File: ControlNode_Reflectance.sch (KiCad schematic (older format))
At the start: 0 parts

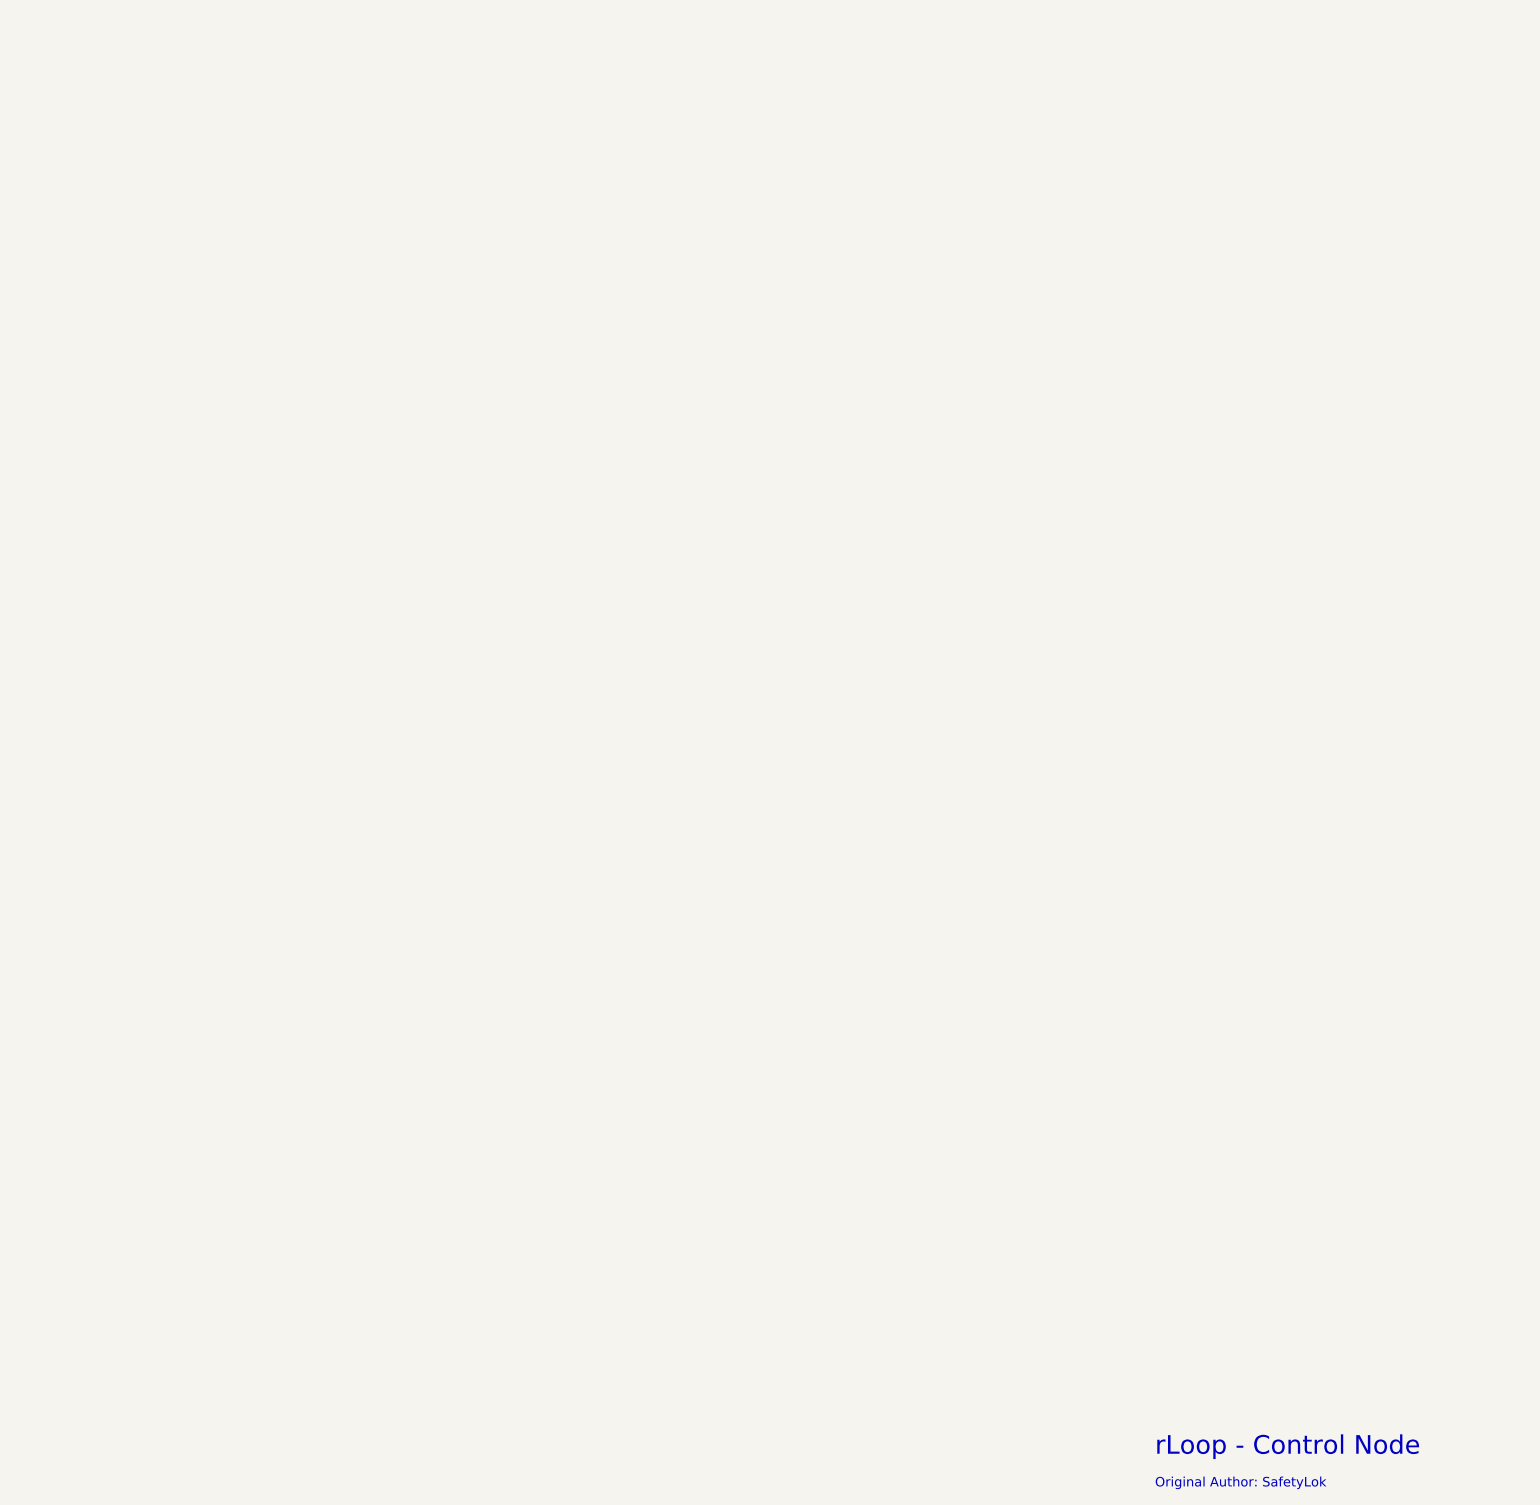
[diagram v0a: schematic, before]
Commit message: Update height sensors.
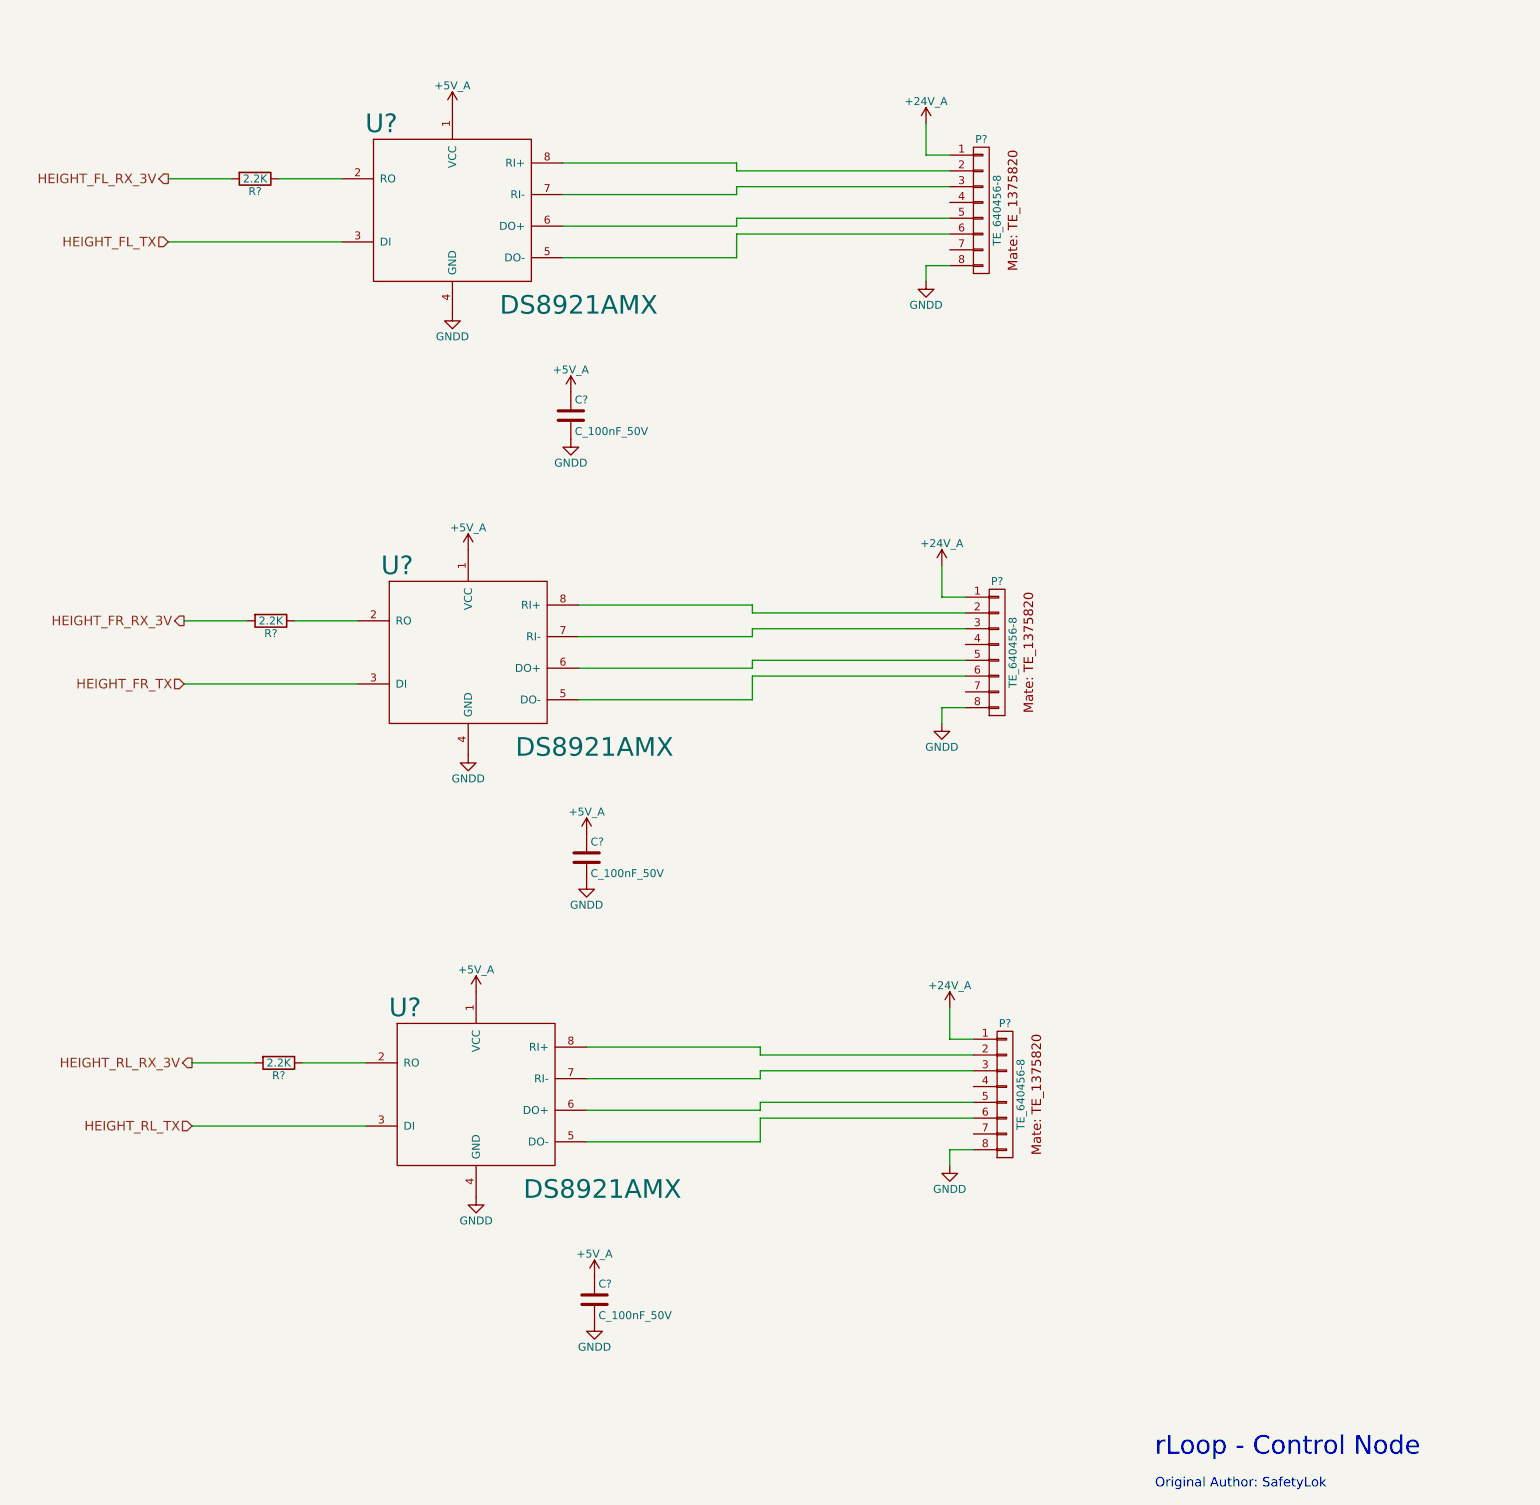
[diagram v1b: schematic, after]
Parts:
- added C? (x3): C_100nF_50V, RLOOP_FOOTPRINTS:rLoop_C_0603, symbol C_100nF_50V
- added P? (x3): TE_640456-8, RLOOP_FOOTPRINTS:rLoop_TE640456-8, symbol TE_640456-8
- added R? (x3): 2.2K, RLOOP_FOOTPRINTS:rLoop_R_0603, symbol 2.2K
- added U? (x3): DS8921AMX, RLOOP_FOOTPRINTS:rLoop_SOIC8, symbol DS8921AMX
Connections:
- new net: P?.2 (P2), U?.8 (RI+) (x3)
- new net: P?.3 (P3), U?.7 (RI-) (x3)
- new net: P?.5 (P5), U?.6 (DO+) (x3)
- new net: P?.6 (P6), U?.5 (DO-) (x3)
- new net: R?.1, U?.2 (RO) (x3)
- new net +5V: C?.1, C?.1, C?.1, P?.1 (P1), P?.1 (P1), P?.1 (P1), U?.1 (VCC), U?.1 (VCC), U?.1 (VCC)
- new net GNDD: C?.2, C?.2, C?.2, P?.8 (P8), P?.8 (P8), P?.8 (P8), U?.4 (GND), U?.4 (GND), U?.4 (GND)
- new net HEIGHT_FL_RX_3V: R?.2
- new net HEIGHT_FL_TX: U?.3 (DI)
- new net HEIGHT_FR_RX_3V: R?.2
- new net HEIGHT_FR_TX: U?.3 (DI)
- new net HEIGHT_RL_RX_3V: R?.2
- new net HEIGHT_RL_TX: U?.3 (DI)

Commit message: Release 1
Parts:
- removed C? (x3): C_100nF_50V, RLOOP_FOOTPRINTS:rLoop_C_0603, symbol C_100nF_50V
- removed P? (x3): TE_640456-8, RLOOP_FOOTPRINTS:rLoop_TE640456-8, symbol TE_640456-8
- removed R? (x3): 2.2K, RLOOP_FOOTPRINTS:rLoop_R_0603, symbol 2.2K
- removed U? (x3): DS8921AMX, RLOOP_FOOTPRINTS:rLoop_SOIC8, symbol DS8921AMX
- added C?: C_100nF_50V, RLOOP_FOOTPRINTS:rLoop_C_0603, symbol C_100nF_50V
- added P? (x3): TE_640456-8, RLOOP_FOOTPRINTS:rLoop_TE640456-8, symbol TE_640456-8
- added R? (x3): 2.2K, RLOOP_FOOTPRINTS:rLoop_R_0603, symbol 2.2K
- added U?: SN74HCT14PWR, RLOOP_FOOTPRINTS:rLoop_TSSOP14, symbol SN74HCT14PWR
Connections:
- net labels added: FRONT_SIG_Q1, FRONT_SIG_Q2, MID_SIG_Q1, MID_SIG_Q2, REAR_SIG_Q1, REAR_SIG_Q2, REFLECT_F, REFLECT_M, REFLECT_R
- net labels removed: HEIGHT_FL_RX_3V, HEIGHT_FL_TX, HEIGHT_FR_RX_3V, HEIGHT_FR_TX, HEIGHT_RL_RX_3V, HEIGHT_RL_TX
- wire segments 57 -> 41
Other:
- note added: "Assume Q2 switches to +UB\nAssume Q1 switches to 0V"
- note added: "FRONT Reflect Sensor"
- note added: "MID Reflect Sensor"
- note added: "REAR Reflect Sensor"

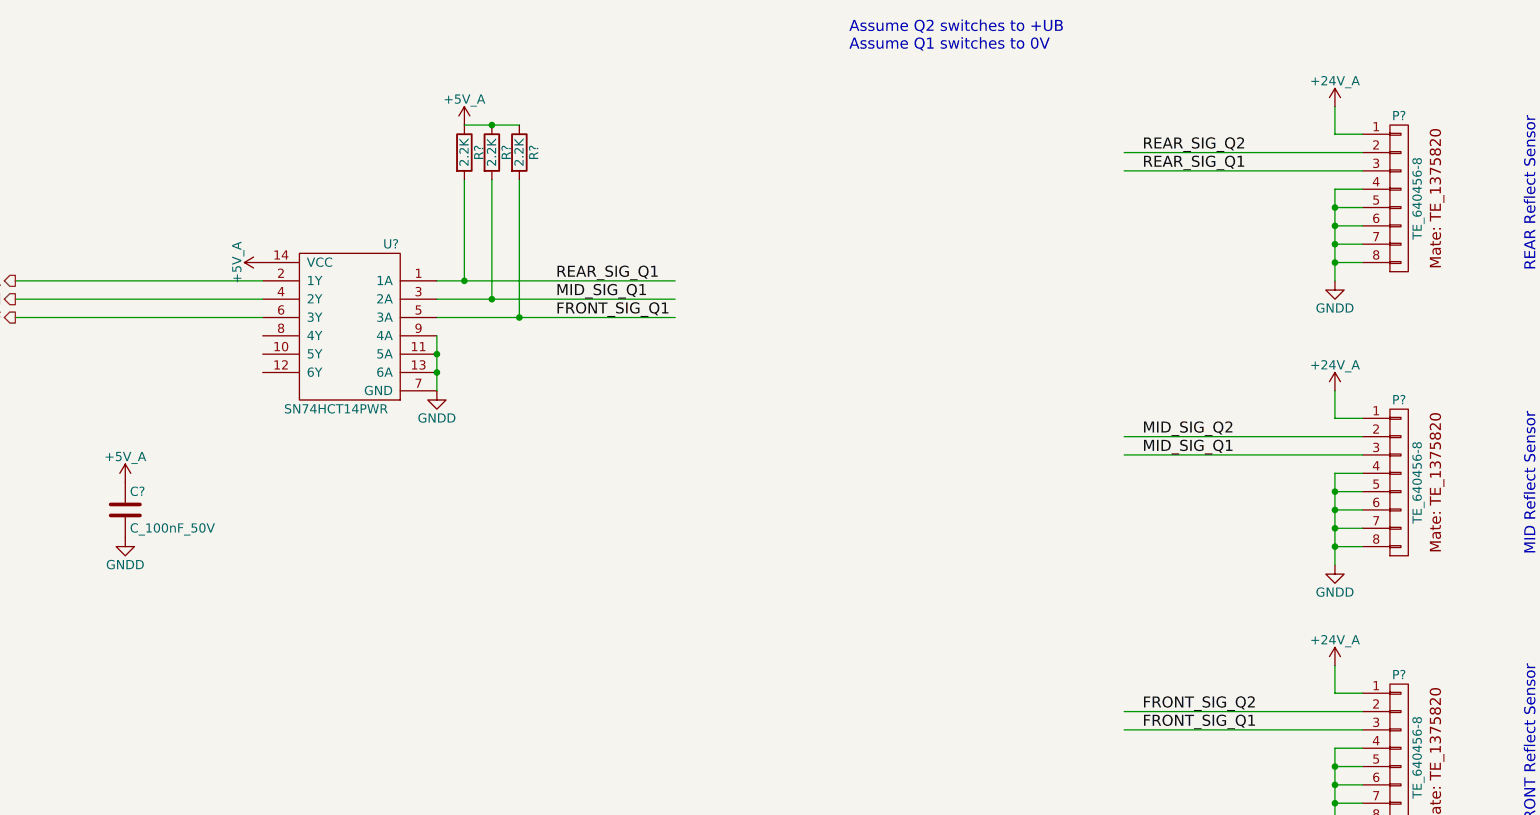
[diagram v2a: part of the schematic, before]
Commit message: Update 10K pullups, 100R on RS422's and additional bypass caps.
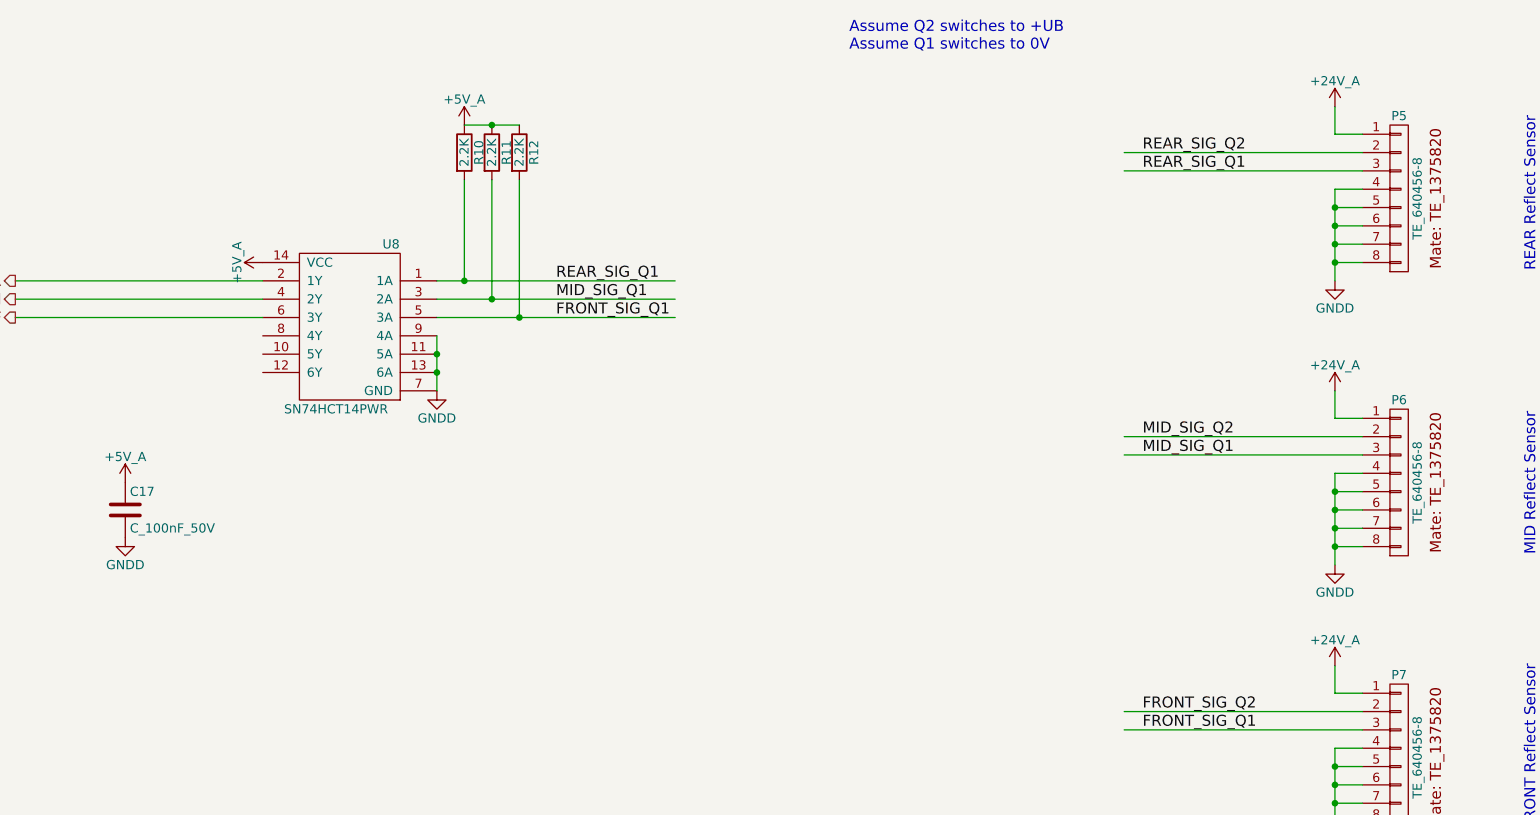
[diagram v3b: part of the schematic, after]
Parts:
- gave numbers to parts that had none: 8
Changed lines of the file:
@@
 REFLECT_F
 $Comp
-L TE_640456-8 P?
+L TE_640456-8 P5
 U 1 1 575E338A
 P 13200 1650
-F 0 "P?" H 13250 1700 50  0000 C CNN
+F 0 "P5" H 13250 1700 50  0000 C CNN
 F 1 "TE_640456-8" V 13350 1250 50  0000 C CNN
 F 2 "RLOOP_FOOTPRINTS:rLoop_TE640456-8" H 13250 1250 50  0001 C CNN
@@
 $EndComp
 $Comp
-L TE_640456-8 P?
+L TE_640456-8 P6
 U 1 1 575E33DD
 P 13200 3200
-F 0 "P?" H 13250 3250 50  0000 C CNN
+F 0 "P6" H 13250 3250 50  0000 C CNN
 F 1 "TE_640456-8" V 13350 2800 50  0000 C CNN
 F 2 "RLOOP_FOOTPRINTS:rLoop_TE640456-8" H 13250 2800 50  0001 C CNN
@@
 $EndComp
 $Comp
-L TE_640456-8 P?
+L TE_640456-8 P7
 U 1 1 575E3435
 P 13200 4700
-F 0 "P?" H 13250 4750 50  0000 C CNN
+F 0 "P7" H 13250 4750 50  0000 C CNN
 F 1 "TE_640456-8" V 13350 4300 50  0000 C CNN
 F 2 "RLOOP_FOOTPRINTS:rLoop_TE640456-8" H 13250 4300 50  0001 C CNN
@@
 FRONT Reflect Sensor
 $Comp
-L +24V_A #PWR?
+L +24V_A #PWR69
 U 1 1 575E3659
 P 12900 1550
-F 0 "#PWR?" H 12900 1400 50  0001 C CNN
+F 0 "#PWR69" H 12900 1400 50  0001 C CNN
 F 1 "+24V_A" H 12900 1690 50  0000 C CNN
 F 2 "" H 12900 1550 60  0000 C CNN
@@
 	12900 1700 13050 1700
 $Comp
-L +24V_A #PWR?
+L +24V_A #PWR71
 U 1 1 575E3676
 P 12900 3100
-F 0 "#PWR?" H 12900 2950 50  0001 C CNN
+F 0 "#PWR71" H 12900 2950 50  0001 C CNN
 F 1 "+24V_A" H 12900 3240 50  0000 C CNN
 F 2 "" H 12900 3100 60  0000 C CNN
@@
 	12900 3250 13050 3250
 $Comp
-L +24V_A #PWR?
+L +24V_A #PWR73
 U 1 1 575E368F
 P 12900 4600
-F 0 "#PWR?" H 12900 4450 50  0001 C CNN
+F 0 "#PWR73" H 12900 4450 50  0001 C CNN
 F 1 "+24V_A" H 12900 4740 50  0000 C CNN
 F 2 "" H 12900 4600 60  0000 C CNN
@@
 REAR_SIG_Q1
 $Comp
-L GNDD #PWR?
+L GNDD #PWR70
 U 1 1 575E36D4
 P 12900 2500
-F 0 "#PWR?" H 12900 2250 50  0001 C CNN
+F 0 "#PWR70" H 12900 2250 50  0001 C CNN
 F 1 "GNDD" H 12900 2350 50  0000 C CNN
 F 2 "" H 12900 2500 50  0000 C CNN
@@
 MID_SIG_Q1
 $Comp
-L GNDD #PWR?
+L GNDD #PWR72
 U 1 1 575E37A8
 P 12900 4050
-F 0 "#PWR?" H 12900 3800 50  0001 C CNN
+F 0 "#PWR72" H 12900 3800 50  0001 C CNN
 F 1 "GNDD" H 12900 3900 50  0000 C CNN
 F 2 "" H 12900 4050 50  0000 C CNN
@@
 FRONT_SIG_Q1
 $Comp
-L GNDD #PWR?
+L GNDD #PWR74
 U 1 1 575E37C4
 P 12900 5550
-F 0 "#PWR?" H 12900 5300 50  0001 C CNN
+F 0 "#PWR74" H 12900 5300 50  0001 C CNN
 F 1 "GNDD" H 12900 5400 50  0000 C CNN
 F 2 "" H 12900 5550 50  0000 C CNN
@@
 Connection ~ 12900 5450
 $Comp
-L 2.2K R?
+L 2.2K R10
 U 1 1 575E3A5A
 P 8150 1800
-F 0 "R?" V 8230 1800 50  0000 C CNN
+F 0 "R10" V 8230 1800 50  0000 C CNN
 F 1 "2.2K" V 8150 1800 50  0000 C CNN
 F 2 "RLOOP_FOOTPRINTS:rLoop_R_0603" V 8080 1800 50  0001 C CNN
@@
 Assume Q2 switches to +UB\nAssume Q1 switches to 0V
 $Comp
-L SN74HCT14PWR U?
+L SN74HCT14PWR U8
 U 1 1 575E4353
 P 7800 2350
-F 0 "U?" H 7850 2400 50  0000 C CNN
+F 0 "U8" H 7850 2400 50  0000 C CNN
 F 1 "SN74HCT14PWR" H 8150 1500 50  0000 C CNN
 F 2 "RLOOP_FOOTPRINTS:rLoop_TSSOP14" H 7800 1550 50  0001 C CNN
@@
 $EndComp
 $Comp
-L +5V_A #PWR?
+L +5V_A #PWR66
 U 1 1 575E4392
 P 7050 2400
-F 0 "#PWR?" H 7050 2250 50  0001 C CNN
+F 0 "#PWR66" H 7050 2250 50  0001 C CNN
 F 1 "+5V_A" H 7050 2540 50  0000 C CNN
 F 2 "" H 7050 2400 60  0000 C CNN
@@
 $EndComp
 $Comp
-L GNDD #PWR?
+L GNDD #PWR67
 U 1 1 575E43B0
 P 8000 3100
-F 0 "#PWR?" H 8000 2850 50  0001 C CNN
+F 0 "#PWR67" H 8000 2850 50  0001 C CNN
 F 1 "GNDD" H 8000 2950 50  0000 C CNN
 F 2 "" H 8000 3100 50  0000 C CNN
@@
 $EndComp
 $Comp
-L C_100nF_50V C?
+L C_100nF_50V C17
 U 1 1 575E43CE
 P 6300 3750
-F 0 "C?" H 6325 3850 50  0000 L CNN
+F 0 "C17" H 6325 3850 50  0000 L CNN
 F 1 "C_100nF_50V" H 6325 3650 50  0000 L CNN
 F 2 "RLOOP_FOOTPRINTS:rLoop_C_0603" H 6338 3600 50  0001 C CNN
@@
 $EndComp
 $Comp
-L +5V_A #PWR?
+L +5V_A #PWR64
 U 1 1 575E43FF
 P 6300 3600
-F 0 "#PWR?" H 6300 3450 50  0001 C CNN
+F 0 "#PWR64" H 6300 3450 50  0001 C CNN
 F 1 "+5V_A" H 6300 3740 50  0000 C CNN
 F 2 "" H 6300 3600 60  0000 C CNN
@@
 $EndComp
 $Comp
-L GNDD #PWR?
+L GNDD #PWR65
 U 1 1 575E4463
 P 6300 3900
-F 0 "#PWR?" H 6300 3650 50  0001 C CNN
+F 0 "#PWR65" H 6300 3650 50  0001 C CNN
 F 1 "GNDD" H 6300 3750 50  0000 C CNN
 F 2 "" H 6300 3900 50  0000 C CNN
@@
 	9300 2700 8000 2700
 $Comp
-L 2.2K R?
+L 2.2K R11
 U 1 1 575E4702
 P 8300 1800
-F 0 "R?" V 8380 1800 50  0000 C CNN
+F 0 "R11" V 8380 1800 50  0000 C CNN
 F 1 "2.2K" V 8300 1800 50  0000 C CNN
 F 2 "RLOOP_FOOTPRINTS:rLoop_R_0603" V 8230 1800 50  0001 C CNN
@@
 $EndComp
 $Comp
-L 2.2K R?
+L 2.2K R12
 U 1 1 575E471F
 P 8450 1800
-F 0 "R?" V 8530 1800 50  0000 C CNN
+F 0 "R12" V 8530 1800 50  0000 C CNN
 F 1 "2.2K" V 8450 1800 50  0000 C CNN
 F 2 "RLOOP_FOOTPRINTS:rLoop_R_0603" V 8380 1800 50  0001 C CNN
@@
 Connection ~ 8450 2700
 $Comp
-L +5V_A #PWR?
+L +5V_A #PWR68
 U 1 1 575E488D
 P 8150 1650
-F 0 "#PWR?" H 8150 1500 50  0001 C CNN
+F 0 "#PWR68" H 8150 1500 50  0001 C CNN
 F 1 "+5V_A" H 8150 1790 50  0000 C CNN
 F 2 "" H 8150 1650 60  0000 C CNN
